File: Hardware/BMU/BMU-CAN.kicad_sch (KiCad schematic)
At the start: 4 parts, among them U3 TCAN334G

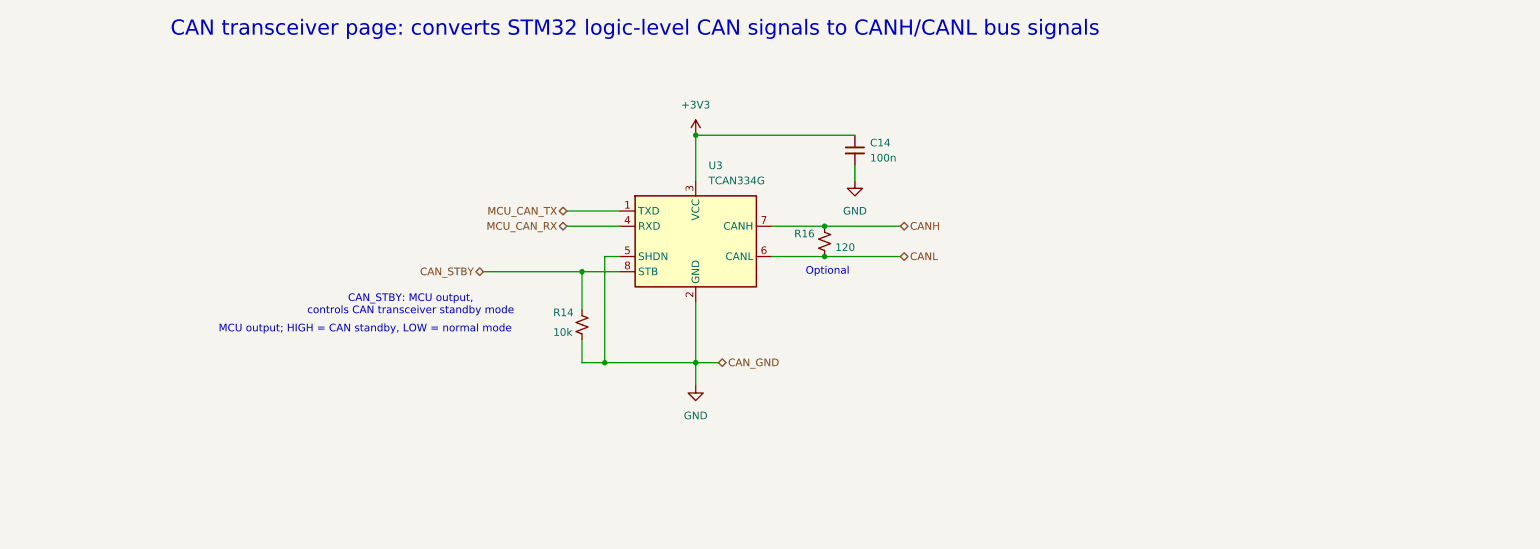
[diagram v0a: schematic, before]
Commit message: change CAN
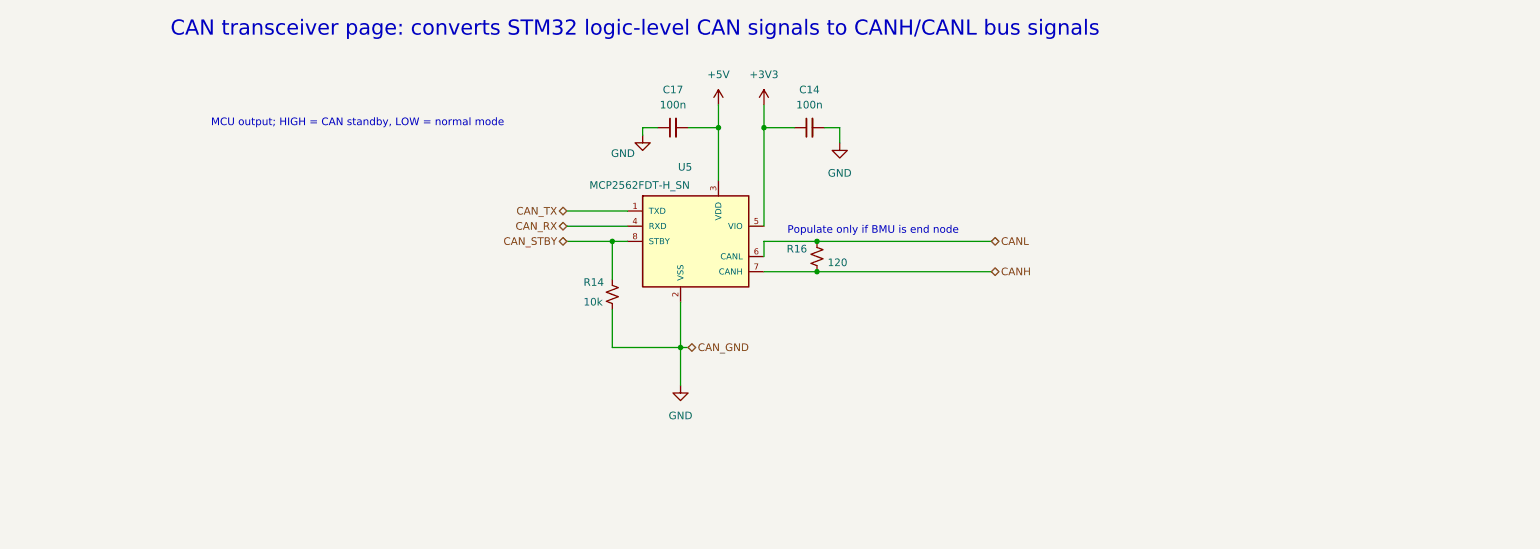
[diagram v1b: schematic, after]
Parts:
- removed U3: TCAN334G, symbol Interface_CAN_LIN:TCAN334G
- added C17: 100n, symbol Device:C_Small
- added U5: MCP2562FDT-H_SN, MCP2562FDT-H_SN:SOIC127P600X175-8N, symbol MCP2562FDT-H_SN:MCP2562FDT-H_SN
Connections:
- net +3V3: now also U5.5 (VIO)
- net CANH: now also R16.2, U5.7 (CANH); no longer R16.1
- net CANL: now also R16.1, U5.6 (CANL); no longer R16.2
- net CAN_STBY: now also U5.8 (STBY)
- net GND: now also C17.1, U5.2 (VSS)
- new net +5V: C17.2, U5.3 (VDD)
- new net CAN_RX: U5.4 (RXD)
- new net CAN_TX: U5.1 (TXD)
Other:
- note added: "Populate only if BMU is end node"
- note removed: "CAN_STBY: MCU output, controls CAN transceiver standby mode"
- note removed: "Optional"
- moved on the sheet: C14, R14, R16

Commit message: add comment
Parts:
- added CR1: ESDCAN03-2BWY, SOT323-3L_STM, symbol ESDCAN03-2BWY:ESDCAN03-2BWY
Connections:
- net CANH: now also CR1.1
- net CANL: now also CR1.2
- net GND: now also CR1.3
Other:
- note added: "CAN_STBY: MCU output; HIGH = CAN standby, LOW = normal mode"
- note removed: "MCU output; HIGH = CAN standby, LOW = normal mode"
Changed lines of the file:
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@@
 		(company "VIKING MOTOR SPORTS (VMS)")
 	)
-	(text "MCU output; HIGH = CAN standby, LOW = normal mode"
+	(text "CAN_STBY: MCU output; \nHIGH = CAN standby, LOW = normal mode"
 		(exclude_from_sim no)
-		(at 119.888 97.028 0)
+		(at 128.016 120.65 0)
 		(effects
 			(font
@@
 	)
 	(junction
-		(at 196.85 116.84)
+		(at 196.85 121.92)
 		(diameter 0)
 		(color 0 0 0 0)
@@
 	)
 	(junction
+		(at 207.01 116.84)
+		(diameter 0)
+		(color 0 0 0 0)
+	)
+	(junction
 		(at 180.34 97.79)
+		(diameter 0)
+		(color 0 0 0 0)
+	)
+	(junction
+		(at 196.85 116.84)
+		(diameter 0)
+		(color 0 0 0 0)
+	)
+	(junction
+		(at 209.55 121.92)
 		(diameter 0)
 		(color 0 0 0 0)
@@
 	)
 	(junction
-		(at 196.85 121.92)
-		(diameter 0)
-		(color 0 0 0 0)
-	)
-	(junction
 		(at 162.56 116.84)
 		(diameter 0)
@@
 	(wire
 		(pts
-			(xy 226.06 121.92) (xy 196.85 121.92)
+			(xy 245.11 121.92) (xy 209.55 121.92)
 		)
 		(stroke
@@
 	(wire
 		(pts
+			(xy 209.55 121.92) (xy 209.55 133.35)
+		)
+		(stroke
+			(width 0)
+			(type default)
+		)
+	)
+	(wire
+		(pts
 			(xy 154.94 116.84) (xy 162.56 116.84)
 		)
@@
 	(wire
 		(pts
+			(xy 209.55 138.43) (xy 207.01 138.43)
+		)
+		(stroke
+			(width 0)
+			(type default)
+		)
+	)
+	(wire
+		(pts
 			(xy 187.96 121.92) (xy 196.85 121.92)
 		)
@@
 	(wire
 		(pts
-			(xy 226.06 116.84) (xy 196.85 116.84)
+			(xy 245.11 116.84) (xy 207.01 116.84)
+		)
+		(stroke
+			(width 0)
+			(type default)
+		)
+	)
+	(wire
+		(pts
+			(xy 207.01 116.84) (xy 207.01 138.43)
 		)
 		(stroke
@@
 	(wire
 		(pts
+			(xy 196.85 116.84) (xy 207.01 116.84)
+		)
+		(stroke
+			(width 0)
+			(type default)
+		)
+	)
+	(wire
+		(pts
 			(xy 167.64 99.06) (xy 167.64 97.79)
 		)
@@
 		(pts
 			(xy 175.26 134.62) (xy 173.99 134.62)
+		)
+		(stroke
+			(width 0)
+			(type default)
+		)
+	)
+	(wire
+		(pts
+			(xy 196.85 121.92) (xy 209.55 121.92)
 		)
 		(stroke
@@
 	(hierarchical_label "CANL"
 		(shape bidirectional)
-		(at 226.06 116.84 0)
+		(at 245.11 116.84 0)
 		(effects
 			(font
@@
 	(hierarchical_label "CANH"
 		(shape bidirectional)
-		(at 226.06 121.92 0)
+		(at 245.11 121.92 0)
 		(effects
 			(font
@@
 	)
 	(symbol
+		(lib_id "power:GND")
+		(at 247.65 135.89 0)
+		(unit 1)
+		(body_style 1)
+		(exclude_from_sim no)
+		(in_bom yes)
+		(on_board yes)
+		(in_pos_files yes)
+		(dnp no)
+		(fields_autoplaced yes)
+		(property "Reference" "#PWR028"
+			(at 247.65 142.24 0)
+			(hide yes)
+			(show_name no)
+			(do_not_autoplace no)
+			(effects
+				(font
+					(size 1.27 1.27)
+				)
+			)
+		)
+		(property "Value" "GND"
+			(at 247.65 140.97 0)
+			(show_name no)
+			(do_not_autoplace no)
+			(effects
+				(font
+					(size 1.27 1.27)
+				)
+			)
+		)
+		(property "Footprint" ""
+			(at 247.65 135.89 0)
+			(hide yes)
+			(show_name no)
+			(do_not_autoplace no)
+			(effects
+				(font
+					(size 1.27 1.27)
+				)
+			)
+		)
+		(property "Datasheet" ""
+			(at 247.65 135.89 0)
+			(hide yes)
+			(show_name no)
+			(do_not_autoplace no)
+			(effects
+				(font
+					(size 1.27 1.27)
+				)
+			)
+		)
+		(property "Description" "Power symbol creates a global label with name \"GND\" , ground"
+			(at 247.65 135.89 0)
+			(hide yes)
+			(show_name no)
+			(do_not_autoplace no)
+			(effects
+				(font
+					(size 1.27 1.27)
+				)
+			)
+		)
+		(pin "1"
+		)
+		(instances
+			(project "BMU"
+				(path "/efb70416-ce55-4766-98ba-c3d23efcccb1/ebb995bd-0019-4c04-a0dd-2962c6aaae17"
+					(reference "#PWR028")
+					(unit 1)
+				)
+			)
+		)
+	)
+	(symbol
 		(lib_id "power:+3V3")
 		(at 187.96 93.98 0)
@@
 					(unit 1)
 				)
+			)
+		)
+	)
+	(symbol
+		(lib_id "ESDCAN03-2BWY:ESDCAN03-2BWY")
+		(at 209.55 133.35 0)
+		(unit 1)
+		(body_style 1)
+		(exclude_from_sim no)
+		(in_bom yes)
+		(on_board yes)
+		(in_pos_files yes)
+		(dnp no)
+		(fields_autoplaced yes)
+		(property "Reference" "CR1"
+			(at 228.6 125.73 0)
+			(show_name no)
+			(do_not_autoplace no)
+			(effects
+				(font
+					(size 1.524 1.524)
+				)
+			)
+		)
+		(property "Value" "ESDCAN03-2BWY"
+			(at 228.6 128.27 0)
+			(show_name no)
+			(do_not_autoplace no)
+			(effects
+				(font
+					(size 1.524 1.524)
+				)
+			)
+		)
+		(property "Footprint" "SOT323-3L_STM"
+			(at 209.55 133.35 0)
+			(hide yes)
+			(show_name no)
+			(do_not_autoplace no)
+			(effects
+				(font
+					(size 1.27 1.27)
+					(italic yes)
+				)
+			)
+		)
+		(property "Datasheet" "https://www.st.com/resource/en/datasheet/esdcan03-2bwy.pdf"
+			(at 209.55 133.35 0)
+			(hide yes)
+			(show_name no)
+			(do_not_autoplace no)
+			(effects
+				(font
+					(size 1.27 1.27)
+					(italic yes)
+				)
+			)
+		)
+		(property "Description" ""
+			(at 209.55 133.35 0)
+			(hide yes)
+			(show_name no)
+			(do_not_autoplace no)
+			(effects
+				(font
+					(size 1.27 1.27)
+				)
+			)
+		)
+		(pin "3"
+		)
+		(pin "1"
+		)
+		(pin "2"
+		)
+		(instances
+			(project "BMU"
+				(path "/efb70416-ce55-4766-98ba-c3d23efcccb1/ebb995bd-0019-4c04-a0dd-2962c6aaae17"
+					(reference "CR1")
+					(unit 1)
+				)

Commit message: add footprint
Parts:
- C14, C17: footprint (none) -> Capacitor_SMD:C_0805_2012Metric
- CR1: footprint SOT323-3L_STM -> ESDCAN03-2BWY:SOT323-3L_STM
- R14, R16: footprint (none) -> Resistor_SMD:R_0805_2012Metric
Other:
- moved on the sheet: C14, C17, CR1, R14, R16, U5

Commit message: update
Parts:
- renumbered C14 to C16
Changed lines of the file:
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@@
 		(dnp no)
 		(fields_autoplaced yes)
-		(property "Reference" "C14"
+		(property "Reference" "C16"
 			(at 229.8763 110.49 90)
 			(show_name no)
@@
 			(project "BMU"
 				(path "/efb70416-ce55-4766-98ba-c3d23efcccb1/ebb995bd-0019-4c04-a0dd-2962c6aaae17"
-					(reference "C14")
+					(reference "C16")
 					(unit 1)
 				)

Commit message: update bmu
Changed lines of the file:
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@@
 	(text "CAN transceiver page: converts STM32 logic-level CAN signals to CANH/CANL bus signals"
 		(exclude_from_sim no)
-		(at 200.66 100.33 0)
+		(at 211.582 99.06 0)
 		(effects
 			(font
